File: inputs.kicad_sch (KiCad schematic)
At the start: 36 parts, among them IC1 Trig Cond Socket, U5 MPX4250, U6 SP720

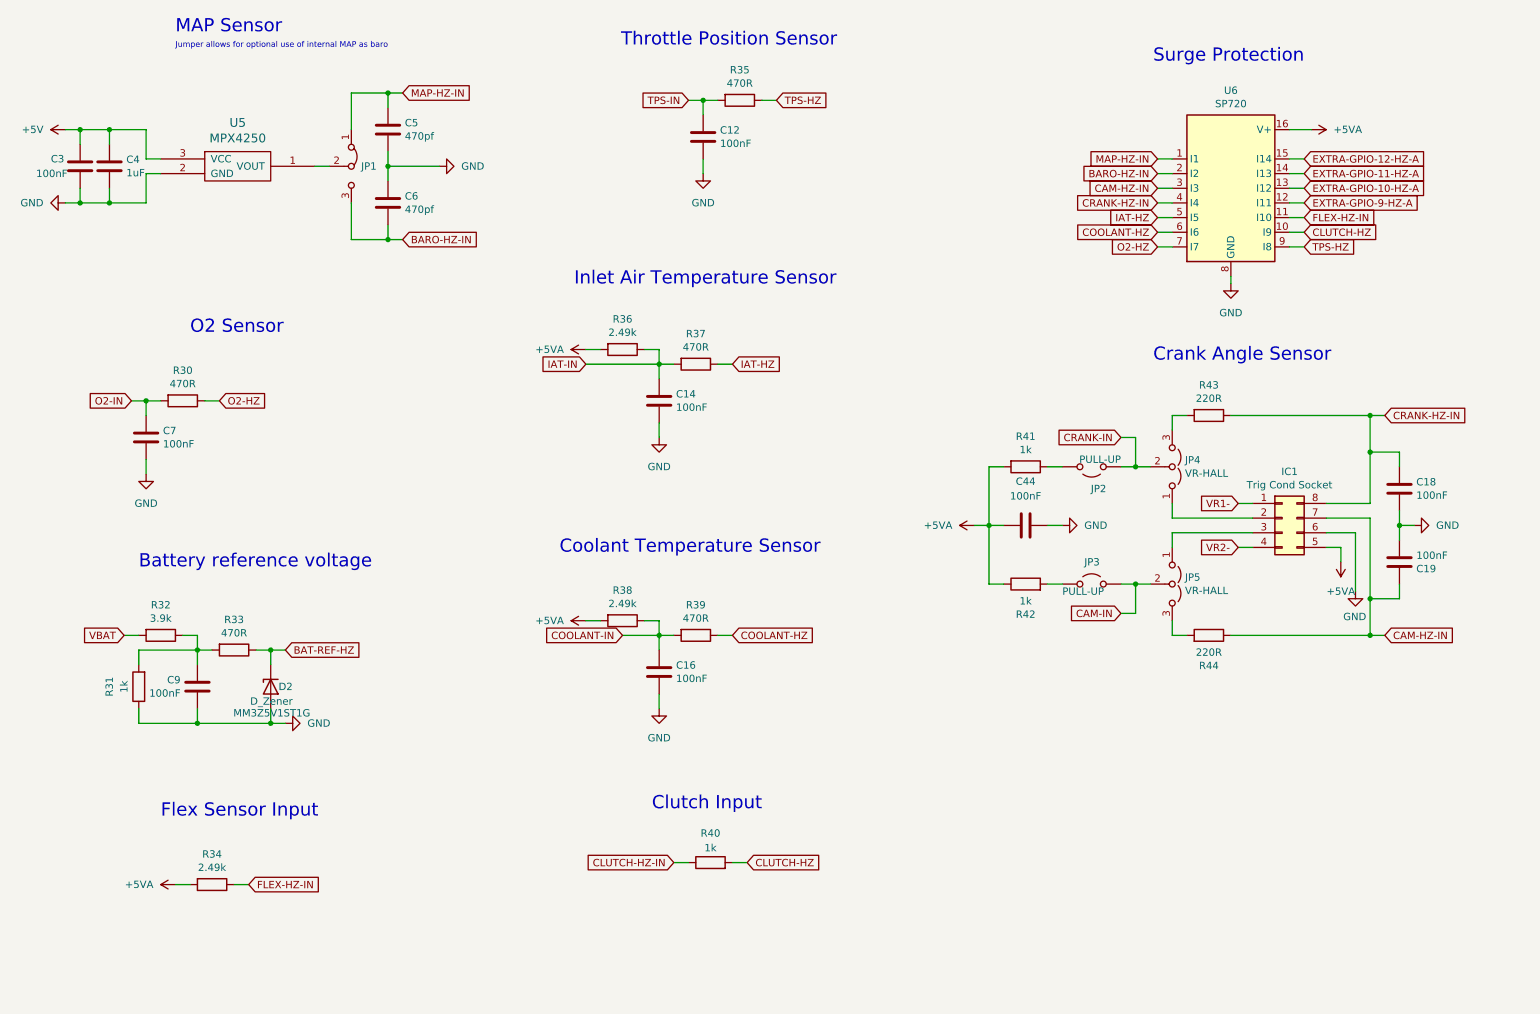
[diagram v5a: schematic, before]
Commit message: Updated reference layout
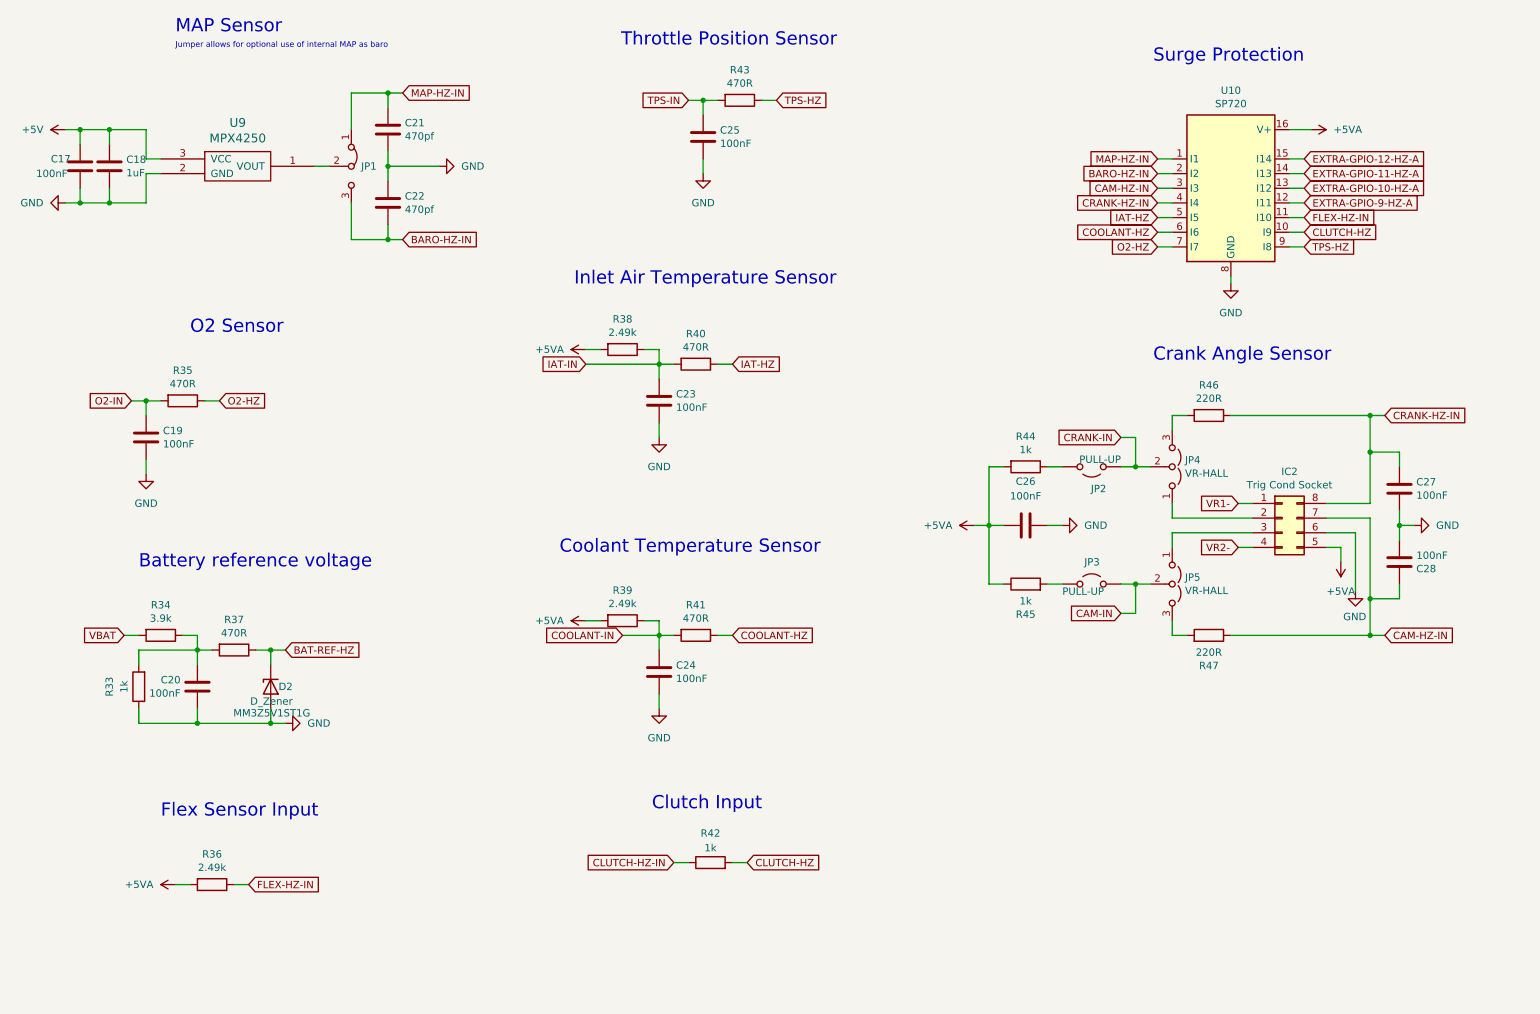
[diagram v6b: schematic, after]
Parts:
- renumbered C3 to C17, C4 to C18, C7 to C19, C9 to C20, C5 to C21, C6 to C22, C14 to C23, C16 to C24, C12 to C25, C44 to C26, C18 to C27, C19 to C28, IC1 to IC2, R31 to R33, R32 to R34, R30 to R35, R34 to R36, R33 to R37, R36 to R38, R38 to R39, R37 to R40, R39 to R41, R40 to R42, R35 to R43, R41 to R44, R42 to R45, R43 to R46, R44 to R47, U6 to U10, U5 to U9
